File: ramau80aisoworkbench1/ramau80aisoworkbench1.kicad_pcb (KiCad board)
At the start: 2 copper layers, 0 parts

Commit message: mx footprints now sit in proper spots for u80
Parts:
- added C1: C_Small, Capacitor_SMD:C_0805_2012Metric, B.Cu at (266.2, 167.9)
- added C2: 22pF, Capacitor_SMD:C_0805_2012Metric, B.Cu at (291.6, 182.8)
- added C3: 22pF, Capacitor_SMD:C_0805_2012Metric, B.Cu at (280.5, 182.1)
- added C4: 0.1uF, Capacitor_SMD:C_0805_2012Metric, B.Cu at (267.7, 178.2)
- added C5: 0.1uF, Capacitor_SMD:C_0805_2012Metric, B.Cu at (262.1, 178.2)
- added C6: 0.1uF, Capacitor_SMD:C_0805_2012Metric, B.Cu at (256.7, 178.2)
- added C7: 0.1uF, Capacitor_SMD:C_0805_2012Metric, B.Cu at (250.2, 178.2)
- added D_A100: D_Small, Diode_SMD:D_SOD-123, B.Cu at (40.8, 85.3)
- added D_B100: D_Small, Diode_SMD:D_SOD-123, B.Cu at (132.1, 102.0)
- added D_BKSP100: D_Small, Diode_SMD:D_SOD-123, B.Cu at (274.6, 35.8)
- added D_C100: D_Small, Diode_SMD:D_SOD-123, B.Cu at (98.4, 92.1)
- added D_CAPS100: D_Small, Diode_SMD:D_SOD-123, B.Cu at (18.6, 83.7)
- added D_COM100: D_Small, Diode_SMD:D_SOD-123, B.Cu at (190.0, 102.0)
- added D_D100: D_Small, Diode_SMD:D_SOD-123, B.Cu at (80.5, 84.5)
- added D_DEL100: D_Small, Diode_SMD:D_SOD-123, B.Cu at (292.9, 54.7)
- added D_DOWN100: D_Small, Diode_SMD:D_SOD-123, B.Cu at (355.9, 119.4)
- added D_E100: D_Small, Diode_SMD:D_SOD-123, B.Cu at (80.5, 65.5)
- added D_END100: D_Small, Diode_SMD:D_SOD-123, B.Cu at (331.8, 54.8)
- added D_ENT100: D_Small, Diode_SMD:D_SOD-123, B.Cu at (268.6, 69.4)
- added D_EQ100: D_Small, Diode_SMD:D_SOD-123, B.Cu at (245.6, 45.6)
- added D_ESC100: D_Small, Diode_SMD:D_SOD-123, B.Cu at (17.8, 6.98)
- added D_F1: D_Small, Diode_SMD:D_SOD-123, B.Cu at (55.9, 6.98)
- added D_F10: D_Small, Diode_SMD:D_SOD-123, B.Cu at (246.4, 6.98)
- added D_F100: D_Small, Diode_SMD:D_SOD-123, B.Cu at (99.5, 82.9)
- added D_F11: D_Small, Diode_SMD:D_SOD-123, B.Cu at (265.4, 6.98)
- added D_F12: D_Small, Diode_SMD:D_SOD-123, B.Cu at (284.5, 6.98)
- added D_F13: D_Small, Diode_SMD:D_SOD-123, B.Cu at (313.1, 6.98)
- added D_F14: D_Small, Diode_SMD:D_SOD-123, B.Cu at (332.1, 6.98)
- added D_F15: D_Small, Diode_SMD:D_SOD-123, B.Cu at (351.2, 6.98)
- added D_F2: D_Small, Diode_SMD:D_SOD-123, B.Cu at (74.9, 6.86)
- added D_F3: D_Small, Diode_SMD:D_SOD-123, B.Cu at (94.0, 6.98)
- added D_F4: D_Small, Diode_SMD:D_SOD-123, B.Cu at (113.0, 6.98)
- added D_F5: D_Small, Diode_SMD:D_SOD-123, B.Cu at (141.6, 6.98)
- added D_F6: D_Small, Diode_SMD:D_SOD-123, B.Cu at (160.7, 6.98)
- added D_F7: D_Small, Diode_SMD:D_SOD-123, B.Cu at (179.7, 6.98)
- added D_F8: D_Small, Diode_SMD:D_SOD-123, B.Cu at (198.8, 6.98)
- added D_F9: D_Small, Diode_SMD:D_SOD-123, B.Cu at (227.3, 6.98)
- added D_FN100: D_Small, Diode_SMD:D_SOD-123, B.Cu at (313.5, 35.8)
- added D_G100: D_Small, Diode_SMD:D_SOD-123, B.Cu at (118.6, 83.7)
- added D_GRV100: D_Small, Diode_SMD:D_SOD-123, B.Cu at (17.8, 35.6)
- added D_H100: D_Small, Diode_SMD:D_SOD-123, B.Cu at (137.6, 84.5)
- added D_HOME100: D_Small, Diode_SMD:D_SOD-123, B.Cu at (331.8, 35.8)
- added D_I100: D_Small, Diode_SMD:D_SOD-123, B.Cu at (178.1, 65.5)
- added D_J100: D_Small, Diode_SMD:D_SOD-123, B.Cu at (156.7, 84.5)
- added D_K100: D_Small, Diode_SMD:D_SOD-123, B.Cu at (177.3, 84.5)
- added D_L100: D_Small, Diode_SMD:D_SOD-123, B.Cu at (196.4, 84.5)
- added D_LALT100: D_Small, Diode_SMD:D_SOD-123, B.Cu at (45.6, 123.4)
- added D_LCTRL100: D_Small, Diode_SMD:D_SOD-123, B.Cu at (16.2, 123.4)
- added D_LEFT100: D_Small, Diode_SMD:D_SOD-123, B.Cu at (336.9, 119.4)
- added D_LOS100: D_Small, Diode_SMD:D_SOD-123, B.Cu at (76.2, 108.8)
- added D_LSFT100: D_Small, Diode_SMD:D_SOD-123, B.Cu at (16.2, 102.0)
- added D_LSQ100: D_Small, Diode_SMD:D_SOD-123, B.Cu at (237.6, 67.8)
- added D_M100: D_Small, Diode_SMD:D_SOD-123, B.Cu at (171.0, 102.8)
- added D_MIN100: D_Small, Diode_SMD:D_SOD-123, B.Cu at (231.3, 46.4)
- added D_N0: D_Small, Diode_SMD:D_SOD-123, B.Cu at (207.5, 46.4)
- added D_N1: D_Small, Diode_SMD:D_SOD-123, B.Cu at (36.8, 35.6)
- added D_N100: D_Small, Diode_SMD:D_SOD-123, B.Cu at (151.1, 102.8)
- added D_N2: D_Small, Diode_SMD:D_SOD-123, B.Cu at (56.7, 45.6)
- added D_N3: D_Small, Diode_SMD:D_SOD-123, B.Cu at (74.9, 44.8)
- added D_N4: D_Small, Diode_SMD:D_SOD-123, B.Cu at (92.4, 46.4)
- added D_N5: D_Small, Diode_SMD:D_SOD-123, B.Cu at (112.2, 46.4)
- added D_N6: D_Small, Diode_SMD:D_SOD-123, B.Cu at (131.3, 46.4)
- added D_N7: D_Small, Diode_SMD:D_SOD-123, B.Cu at (150.3, 46.4)
- added D_N8: D_Small, Diode_SMD:D_SOD-123, B.Cu at (169.4, 46.4)
- added D_N9: D_Small, Diode_SMD:D_SOD-123, B.Cu at (188.4, 46.4)
- added D_O100: D_Small, Diode_SMD:D_SOD-123, B.Cu at (199.5, 65.5)
- added D_P100: D_Small, Diode_SMD:D_SOD-123, B.Cu at (217.8, 65.5)
- added D_PER100: D_Small, Diode_SMD:D_SOD-123, B.Cu at (207.5, 102.8)
- added D_PGDN100: D_Small, Diode_SMD:D_SOD-123, B.Cu at (350.8, 54.8)
- added D_PGUP100: D_Small, Diode_SMD:D_SOD-123, B.Cu at (351.6, 34.9)
- added D_PIPE100: D_Small, Diode_SMD:D_SOD-123, B.Cu at (260.7, 83.7)
- added D_Q100: D_Small, Diode_SMD:D_SOD-123, B.Cu at (51.1, 54.5)
- added D_QUO100: D_Small, Diode_SMD:D_SOD-123, B.Cu at (241.6, 85.3)
- added D_R100: D_Small, Diode_SMD:D_SOD-123, B.Cu at (100.3, 64.7)
- added D_RALT100: D_Small, Diode_SMD:D_SOD-123, B.Cu at (255.9, 122.6)
- added D_RCTRL100: D_Small, Diode_SMD:D_SOD-123, B.Cu at (282.9, 122.6)
- added D_RIGHT100: D_Small, Diode_SMD:D_SOD-123, B.Cu at (375.0, 119.4)
- added D_ROS100: D_Small, Diode_SMD:D_SOD-123, B.Cu at (225.7, 122.6)
- added D_RSFT100: D_Small, Diode_SMD:D_SOD-123, B.Cu at (271.8, 102.8)
- added D_RSQ100: D_Small, Diode_SMD:D_SOD-123, B.Cu at (261.3, 54.4)
- added D_S100: D_Small, Diode_SMD:D_SOD-123, B.Cu at (59.1, 84.5)
- added D_SEMI100: D_Small, Diode_SMD:D_SOD-123, B.Cu at (216.2, 84.5)
- added D_SLASH100: D_Small, Diode_SMD:D_SOD-123, B.Cu at (225.7, 103.6)
- added D_SPACE100: D_Small, Diode_SMD:D_SOD-123, B.Cu at (154.0, 111.9)
- added D_T100: D_Small, Diode_SMD:D_SOD-123, B.Cu at (118.6, 65.5)
- added D_TAB100: D_Small, Diode_SMD:D_SOD-123, B.Cu at (18.6, 65.5)
- added D_TILD100: D_Small, Diode_SMD:D_SOD-123, B.Cu at (34.4, 102.0)
- added D_U100: D_Small, Diode_SMD:D_SOD-123, B.Cu at (158.3, 64.6)
- added D_UP100: D_Small, Diode_SMD:D_SOD-123, B.Cu at (332.6, 92.9)
- added D_V100: D_Small, Diode_SMD:D_SOD-123, B.Cu at (113.8, 102.0)
- added D_W100: D_Small, Diode_SMD:D_SOD-123, B.Cu at (61.4, 65.5)
- added D_X100: D_Small, Diode_SMD:D_SOD-123, B.Cu at (79.4, 92.8)
- added D_Y100: D_Small, Diode_SMD:D_SOD-123, B.Cu at (138.4, 64.7)
- added D_Z100: D_Small, Diode_SMD:D_SOD-123, B.Cu at (54.3, 101.2)
- added F1: 500mA, Fuse:Fuse_1206_3216Metric, B.Cu at (287.7, 167.9)
- added MX_A100: MX-NoLED, MX_Only:MXOnly-1U, F.Cu at (42.9, 76.2)
- added MX_B100: MX-NoLED, MX_Only:MXOnly-1U, F.Cu at (128.6, 95.2)
- added MX_BKSP100: MX-NoLED, MX_Only:MXOnly-1U, F.Cu at (266.7, 38.1)
- added MX_C100: MX-NoLED, MX_Only:MXOnly-1U, F.Cu at (90.5, 95.2)
- added MX_CAPS100: MX-NoLED, MX_Only:MXOnly-1U, F.Cu at (16.7, 76.2)
- added MX_COM100: MX-NoLED, MX_Only:MXOnly-1U, F.Cu at (185.7, 95.2)
- added MX_D100: MX-NoLED, MX_Only:MXOnly-1U, F.Cu at (81.0, 76.2)
- added MX_DEL100: MX-NoLED, MX_Only:MXOnly-1U, F.Cu at (304.8, 57.1)
- added MX_DOWN100: MX-NoLED, MX_Only:MXOnly-1U, F.Cu at (323.9, 114.3)
- added MX_E100: MX-NoLED, MX_Only:MXOnly-1U, F.Cu at (76.2, 57.1)
- added MX_END100: MX-NoLED, MX_Only:MXOnly-1U, F.Cu at (323.9, 57.1)
- added MX_ENT100: MX-ISO-ENT, MX_Only:MXOnly-1U, F.Cu at (276.2, 66.7)
- added MX_EQ100: MX-NoLED, MX_Only:MXOnly-1U, F.Cu at (238.1, 38.1)
- added MX_ESC100: MX-NoLED, MX_Only:MXOnly-1U, F.Cu at (9.53, 9.53)
- added MX_F1: MX-NoLED, MX_Only:MXOnly-1U, F.Cu at (47.6, 9.53)
- added MX_F10: MX-NoLED, MX_Only:MXOnly-1U, F.Cu at (238.1, 9.53)
- added MX_F100: MX-NoLED, MX_Only:MXOnly-1U, F.Cu at (100.0, 76.2)
- added MX_F11: MX-NoLED, MX_Only:MXOnly-1U, F.Cu at (257.2, 9.53)
- added MX_F12: MX-NoLED, MX_Only:MXOnly-1U, F.Cu at (276.2, 9.53)
- added MX_F13: MX-NoLED, MX_Only:MXOnly-1U, F.Cu at (304.8, 9.53)
- added MX_F14: MX-NoLED, MX_Only:MXOnly-1U, F.Cu at (323.9, 9.53)
- added MX_F15: MX-NoLED, MX_Only:MXOnly-1U, F.Cu at (342.9, 9.53)
- added MX_F2: MX-NoLED, MX_Only:MXOnly-1U, F.Cu at (66.7, 9.53)
- added MX_F3: MX-NoLED, MX_Only:MXOnly-1U, F.Cu at (85.7, 9.53)
- added MX_F4: MX-NoLED, MX_Only:MXOnly-1U, F.Cu at (104.8, 9.53)
- added MX_F5: MX-NoLED, MX_Only:MXOnly-1U, F.Cu at (133.3, 9.53)
- added MX_F6: MX-NoLED, MX_Only:MXOnly-1U, F.Cu at (152.4, 9.53)
- added MX_F7: MX-NoLED, MX_Only:MXOnly-1U, F.Cu at (171.4, 9.53)
- added MX_F8: MX-NoLED, MX_Only:MXOnly-1U, F.Cu at (190.5, 9.53)
- added MX_F9: MX-NoLED, MX_Only:MXOnly-1U, F.Cu at (219.1, 9.53)
- added MX_FN100: MX-NoLED, MX_Only:MXOnly-1U, F.Cu at (304.8, 38.1)
- added MX_G100: MX-NoLED, MX_Only:MXOnly-1U, F.Cu at (119.1, 76.2)
- added MX_GRV100: MX-NoLED, MX_Only:MXOnly-1U, F.Cu at (9.53, 38.1)
- added MX_H100: MX-NoLED, MX_Only:MXOnly-1U, F.Cu at (138.1, 76.2)
- added MX_HOME100: MX-NoLED, MX_Only:MXOnly-1U, F.Cu at (323.9, 38.1)
- added MX_I100: MX-NoLED, MX_Only:MXOnly-1U, F.Cu at (171.4, 57.1)
- added MX_J100: MX-NoLED, MX_Only:MXOnly-1U, F.Cu at (157.2, 76.2)
- added MX_K100: MX-NoLED, MX_Only:MXOnly-1U, F.Cu at (176.2, 76.2)
- added MX_L100: MX-NoLED, MX_Only:MXOnly-1U, F.Cu at (195.3, 76.2)
- added MX_LALT100: MX-NoLED, MX_Only:MXOnly-1U, F.Cu at (38.1, 114.3)
- added MX_LCTRL100: MX-NoLED, MX_Only:MXOnly-1U, F.Cu at (14.3, 114.3)
- added MX_LEFT100: MX-NoLED, MX_Only:MXOnly-1U, F.Cu at (304.8, 114.3)
- added MX_LOS100: MX-NoLED, MX_Only:MXOnly-1U, F.Cu at (61.9, 114.3)
- added MX_LSFT100: MX-NoLED, MX_Only:MXOnly-1U, F.Cu at (11.9, 95.2)
- added MX_LSQ100: MX-NoLED, MX_Only:MXOnly-1U, F.Cu at (228.6, 57.1)
- added MX_M100: MX-NoLED, MX_Only:MXOnly-1U, F.Cu at (166.7, 95.2)
- added MX_MIN100: MX-NoLED, MX_Only:MXOnly-1U, F.Cu at (219.1, 38.1)
- added MX_N0: MX-NoLED, MX_Only:MXOnly-1U, F.Cu at (200.0, 38.1)
- added MX_N1: MX-NoLED, MX_Only:MXOnly-1U, F.Cu at (28.6, 38.1)
- added MX_N100: MX-NoLED, MX_Only:MXOnly-1U, F.Cu at (147.6, 95.2)
- added MX_N2: MX-NoLED, MX_Only:MXOnly-1U, F.Cu at (47.6, 38.1)
- added MX_N3: MX-NoLED, MX_Only:MXOnly-1U, F.Cu at (66.7, 38.1)
- added MX_N4: MX-NoLED, MX_Only:MXOnly-1U, F.Cu at (85.7, 38.1)
- added MX_N5: MX-NoLED, MX_Only:MXOnly-1U, F.Cu at (104.8, 38.1)
- added MX_N6: MX-NoLED, MX_Only:MXOnly-1U, F.Cu at (123.8, 38.1)
- added MX_N7: MX-NoLED, MX_Only:MXOnly-1U, F.Cu at (142.9, 38.1)
- added MX_N8: MX-NoLED, MX_Only:MXOnly-1U, F.Cu at (161.9, 38.1)
- added MX_N9: MX-NoLED, MX_Only:MXOnly-1U, F.Cu at (181.0, 38.1)
- added MX_O100: MX-NoLED, MX_Only:MXOnly-1U, F.Cu at (190.5, 57.1)
- added MX_P100: MX-NoLED, MX_Only:MXOnly-1U, F.Cu at (209.6, 57.1)
- added MX_PER100: MX-NoLED, MX_Only:MXOnly-1U, F.Cu at (204.8, 95.2)
- added MX_PGDN100: MX-NoLED, MX_Only:MXOnly-1U, F.Cu at (342.9, 57.1)
- added MX_PGUP100: MX-NoLED, MX_Only:MXOnly-1U, F.Cu at (342.9, 38.1)
- added MX_PIPE100: MX-NoLED, MX_Only:MXOnly-1U, F.Cu at (252.4, 76.2)
- added MX_Q100: MX-NoLED, MX_Only:MXOnly-1U, F.Cu at (38.1, 57.1)
- added MX_QUO100: MX-NoLED, MX_Only:MXOnly-1U, F.Cu at (233.4, 76.2)
- added MX_R100: MX-NoLED, MX_Only:MXOnly-1U, F.Cu at (95.2, 57.1)
- added MX_RALT100: MX-NoLED, MX_Only:MXOnly-1U, F.Cu at (247.7, 114.3)
- added MX_RCTRL100: MX-NoLED, MX_Only:MXOnly-1U, F.Cu at (271.5, 114.3)
- added MX_RIGHT100: MX-NoLED, MX_Only:MXOnly-1U, F.Cu at (342.9, 114.3)
- added MX_ROS100: MX-NoLED, MX_Only:MXOnly-1U, F.Cu at (223.8, 114.3)
- added MX_RSFT100: MX-NoLED, MX_Only:MXOnly-1U, F.Cu at (257.2, 95.2)
- added MX_RSQ100: MX-NoLED, MX_Only:MXOnly-1U, F.Cu at (247.7, 57.1)
- added MX_S100: MX-NoLED, MX_Only:MXOnly-1U, F.Cu at (61.9, 76.2)
- added MX_SEMI100: MX-NoLED, MX_Only:MXOnly-1U, F.Cu at (214.3, 76.2)
- added MX_SLASH100: MX-NoLED, MX_Only:MXOnly-1U, F.Cu at (223.8, 95.2)
- added MX_SPACE100: MX-NoLED, MX_Only:MXOnly-1U, F.Cu at (145.3, 114.3)
- added MX_T100: MX-NoLED, MX_Only:MXOnly-1U, F.Cu at (114.3, 57.1)
- added MX_TAB100: MX-NoLED, MX_Only:MXOnly-1U, F.Cu at (14.3, 57.1)
- added MX_TILD100: MX-NoLED, MX_Only:MXOnly-1U, F.Cu at (33.3, 95.2)
- added MX_U100: MX-NoLED, MX_Only:MXOnly-1U, F.Cu at (152.4, 57.1)
- added MX_UP100: MX-NoLED, MX_Only:MXOnly-1U, F.Cu at (323.9, 95.2)
- added MX_V100: MX-NoLED, MX_Only:MXOnly-1U, F.Cu at (109.5, 95.2)
- added MX_W100: MX-NoLED, MX_Only:MXOnly-1U, F.Cu at (57.1, 57.1)
- added MX_X100: MX-NoLED, MX_Only:MXOnly-1U, F.Cu at (71.4, 95.2)
- added MX_Y100: MX-NoLED, MX_Only:MXOnly-1U, F.Cu at (133.3, 57.1)
- added MX_Z100: MX-NoLED, MX_Only:MXOnly-1U, F.Cu at (52.4, 95.2)
- added R1: 22, Resistor_SMD:R_0805_2012Metric, B.Cu at (331.2, 198.8)
- added R2: 22, Resistor_SMD:R_0805_2012Metric, B.Cu at (325.0, 198.8)
- added R3: 10k, Resistor_SMD:R_0805_2012Metric, B.Cu at (273.5, 179.8)
- added R4: 10k, Resistor_SMD:R_0805_2012Metric, B.Cu at (284.5, 160.7)
- added SW1: SW_PUSH, random-keyboard-parts:SKQG-1155865, B.Cu at (293.2, 175.8)
- added U1: ATmega32U4-AU, Package_QFP:TQFP-44_10x10mm_P0.8mm, B.Cu at (275.7, 169.4)
- added USB1: Molex-0548190589, random-keyboard-parts:PJ-3200B-4A-Assembly, F.Cu at (332.9, 173.4)
- added Y1: 16MHz, Crystal:Crystal_SMD_3225-4Pin_3.2x2.5mm, B.Cu at (285.3, 181.4)

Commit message: diodes aligned to switches
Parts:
- moved D_DOWN100 25.0 mm to (332.1, 111.8)
- moved D_LEFT100 25.0 mm to (313.1, 111.8)
- moved D_RIGHT100 25.0 mm to (351.2, 111.8)
- moved D_DEL100 20.2 mm to (313.1, 54.6)
- moved D_A100 15.6 mm to (51.2, 73.7)
- moved D_S100 15.6 mm to (70.2, 73.7)
- moved D_H100 14.0 mm to (146.4, 73.7)
- moved D_D100 14.0 mm to (89.3, 73.7)
- moved D_J100 14.0 mm to (165.5, 73.7)
- moved D_G100 13.4 mm to (127.4, 73.7)
- moved D_LCTRL100 13.3 mm to (22.6, 111.8)
- moved D_LSQ100 13.3 mm to (236.9, 54.6)
- moved D_K100 13.0 mm to (184.5, 73.7)
- moved D_L100 13.0 mm to (203.6, 73.7)
- moved D_F100 12.8 mm to (108.3, 73.7)
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
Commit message: fixed error in footprint assignment. updated switch footprints to use appropriate size, ditched leds
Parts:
- C1: value C_Small -> 1uF
- MX_A100, MX_B100, MX_C100, MX_COM100, MX_D100, MX_DEL100, MX_DOWN100, MX_E100, MX_END100, MX_EQ100, MX_ESC100, MX_F1, MX_F10, MX_F100, MX_F11, MX_F12, MX_F13, MX_F14, MX_F15, MX_F2, MX_F3, MX_F4, MX_F5, MX_F6, MX_F7, MX_F8, MX_F9, MX_FN100, MX_G100, MX_GRV100, MX_H100, MX_HOME100, MX_I100, MX_J100, MX_K100, MX_L100, MX_LALT100, MX_LEFT100, MX_LSQ100, MX_M100, MX_MIN100, MX_N0, MX_N1, MX_N100, MX_N2, MX_N3, MX_N4, MX_N5, MX_N6, MX_N7, MX_N8, MX_N9, MX_O100, MX_P100, MX_PER100, MX_PGDN100, MX_PGUP100, MX_PIPE100, MX_Q100, MX_QUO100, MX_R100, MX_RALT100, MX_RIGHT100, MX_RSQ100, MX_S100, MX_SEMI100, MX_SLASH100, MX_T100, MX_TILD100, MX_U100, MX_UP100, MX_V100, MX_W100, MX_X100, MX_Y100, MX_Z100: footprint MX_Only:MXOnly-1U -> MX_Only:MXOnly-1U-NoLED
- MX_BKSP100: footprint MX_Only:MXOnly-1U -> MX_Only:MXOnly-2U-NoLED
- MX_CAPS100: footprint MX_Only:MXOnly-1U -> MX_Only:MXOnly-1.75U-NoLED
- MX_ENT100: footprint MX_Only:MXOnly-1U -> MX_Only:MXOnly-ISO-ROTATED-NoLED
- MX_LCTRL100, MX_LOS100, MX_RCTRL100, MX_ROS100, MX_TAB100: footprint MX_Only:MXOnly-1U -> MX_Only:MXOnly-1.5U-NoLED
- MX_LSFT100: footprint MX_Only:MXOnly-1U -> MX_Only:MXOnly-1.25U-NoLED
- MX_RSFT100: footprint MX_Only:MXOnly-1U -> MX_Only:MXOnly-2.75U-NoLED
- MX_SPACE100: footprint MX_Only:MXOnly-1U -> MX_Only:MXOnly-7U-NoLED
- USB1: footprint random-keyboard-parts:PJ-3200B-4A-Assembly -> random-keyboard-parts:Molex-0548190589
- moved USB1 388.2 mm to (-23.1, 18.5)
- moved R2 356.0 mm to (14.7, 24.2)
- moved R1 356.0 mm to (20.9, 24.2)
- moved C2 321.6 mm to (24.4, 3.81), turned to 270 degrees
- moved Y1 311.6 mm to (29.2, 3.81), turned to 180 degrees
- moved C3 304.2 mm to (34.0, 3.78), turned to 90 degrees
- moved U1 291.2 mm to (28.4, 15.7)
- moved R4 283.4 mm to (36.8, 22.9), turned to 90 degrees
- moved C7 266.4 mm to (32.3, 24.9), turned to 180 degrees
- moved R3 17.5 mm to (289.9, 185.9)
- moved MX_ENT100 2.38 mm to (273.8, 66.7), turned to 0 degrees
- moved MX_RSFT100 2.38 mm to (259.6, 95.2)

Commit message: re-aligned spacebar. wups.
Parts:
- moved C1 383.3 mm to (-48.9, -50.4)
- moved C4 383.3 mm to (-47.5, -40.1)
- moved C5 383.3 mm to (-53.0, -40.1)
- moved C6 383.3 mm to (-58.4, -40.1)
- moved F1 383.3 mm to (-27.5, -50.4)
- moved R3 383.3 mm to (-25.2, -32.4)
- moved SW1 383.3 mm to (-21.9, -42.5)
- moved D_SPACE100 2.41 mm to (151.1, 111.8)
- moved MX_SPACE100 2.38 mm to (142.9, 114.3)

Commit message: lee. updated to kicad 7. adding usbc library
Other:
- net class Default removed

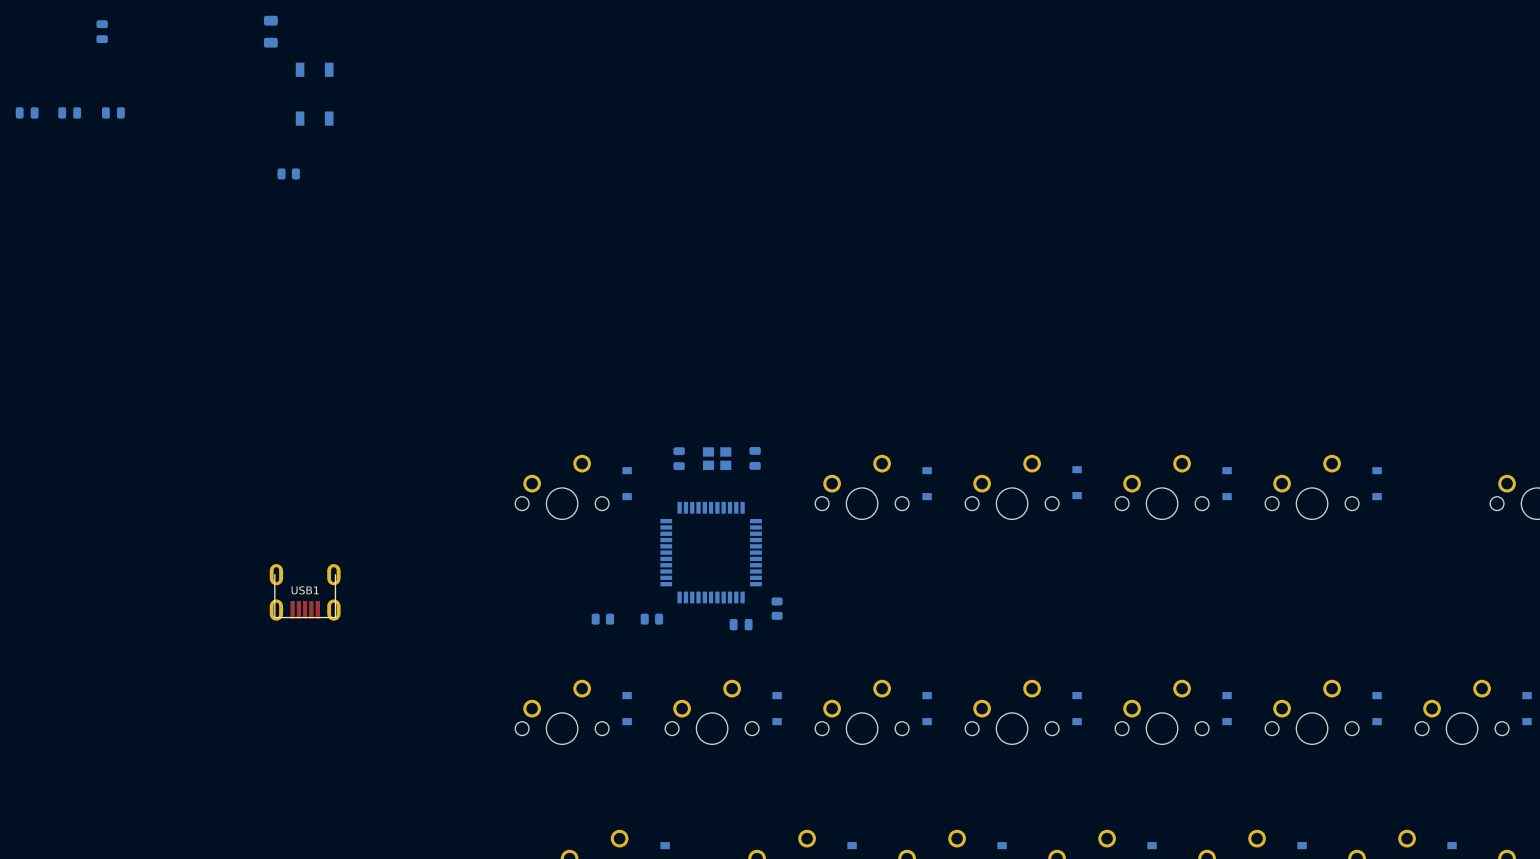
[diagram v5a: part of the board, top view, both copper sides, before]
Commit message: all parts on board! lets make sure the resistors and capacitors are all right and that the ground issue is sorted. then routing
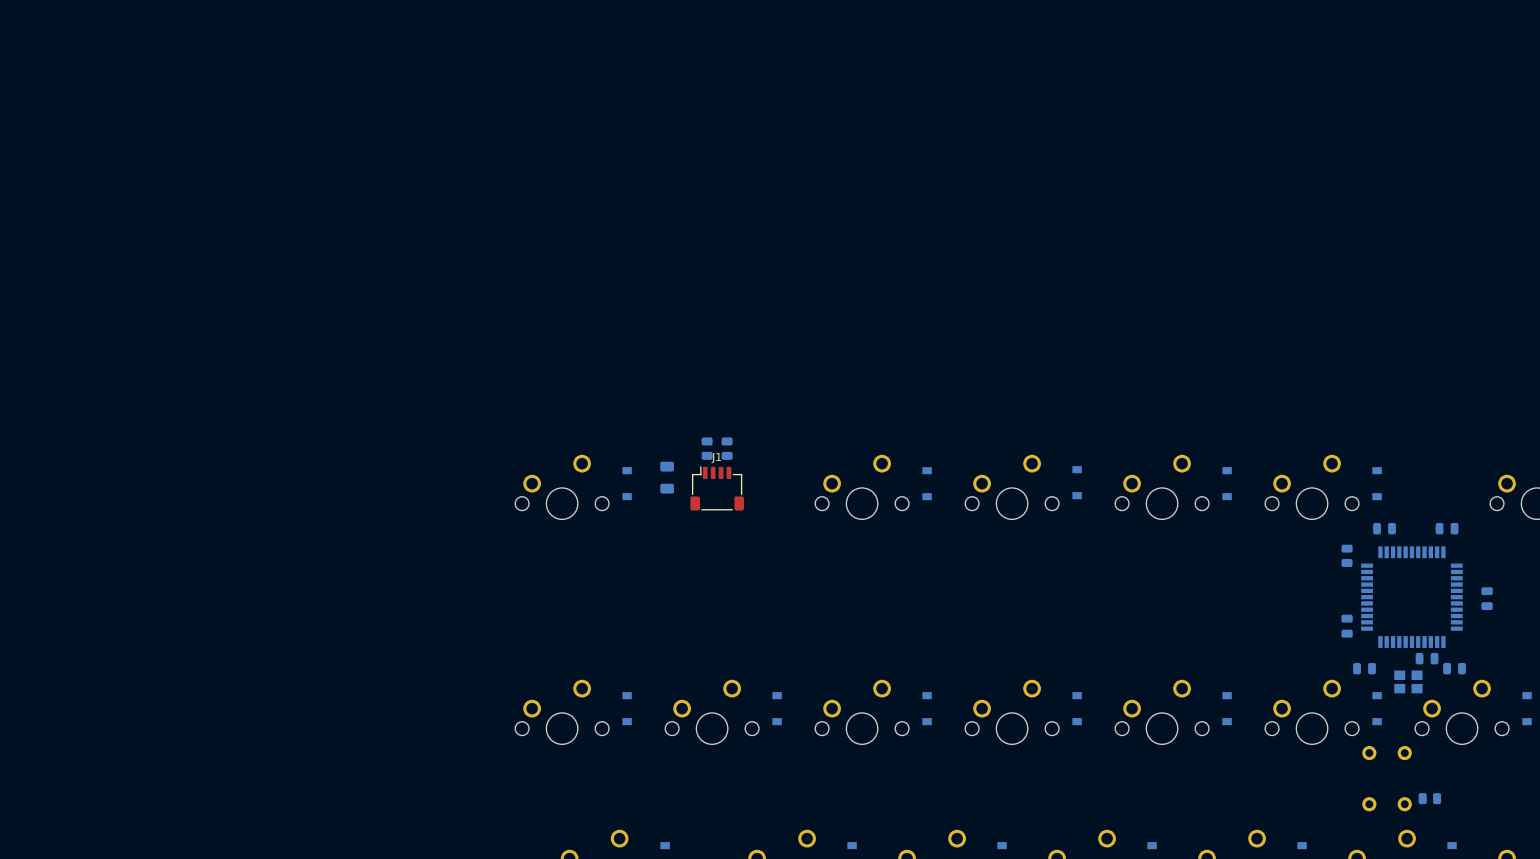
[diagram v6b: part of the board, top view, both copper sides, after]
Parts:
- removed USB1: Molex-0548190589, random-keyboard-parts:Molex-0548190589
- added J1: Conn_01x04_Socket, Connector_JST:JST_SH_SM04B-SRSS-TB_1x04-1MP_P1.00mm_Horizontal, F.Cu at (29.2, 7.62)
- SW1: footprint random-keyboard-parts:SKQG-1155865 -> random-keyboard-parts:PushButton_6x6mm_TH_Pretty
- moved C1 190.1 mm to (127.0, 21.6)
- moved C5 185.8 mm to (119.4, 29.2)
- moved C6 179.9 mm to (109.2, 25.1), turned to 90 degrees
- moved C4 169.9 mm to (114.0, 12.7)
- moved R3 165.2 mm to (119.7, 47.0)
- moved SW1 161.6 mm to (114.3, 44.5), turned to -90 degrees
- moved C2 102.0 mm to (122.9, 30.5), turned to 0 degrees
- moved Y1 92.3 mm to (117.0, 32.2), turned to 0 degrees
- moved C7 90.5 mm to (121.9, 12.7), turned to 0 degrees
- moved U1 89.2 mm to (117.5, 21.4), turned to 180 degrees
- moved C3 81.9 mm to (111.4, 30.5), turned to 0 degrees
- moved F1 75.8 mm to (22.9, 6.22), turned to -90 degrees
- moved R4 72.7 mm to (109.2, 16.2), turned to -90 degrees
- moved R2 26.8 mm to (30.5, 2.54), turned to -90 degrees
- moved R1 22.8 mm to (27.9, 2.54), turned to 90 degrees
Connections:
- U1 pad 1: Net-(U1-Pad1) -> unconnected-(U1-PE6-Pad1)
- U1 pad 10: Net-(U1-Pad10) -> unconnected-(U1-PB2-Pad10)
- U1 pad 11: Net-(U1-Pad11) -> unconnected-(U1-PB3-Pad11)
- U1 pad 12: Net-(U1-Pad12) -> unconnected-(U1-PB7-Pad12)
- U1 pad 18: Net-(U1-Pad18) -> unconnected-(U1-PD0-Pad18)
- U1 pad 19: Net-(U1-Pad19) -> unconnected-(U1-PD1-Pad19)
- U1 pad 20: Net-(U1-Pad20) -> unconnected-(U1-PD2-Pad20)
- U1 pad 21: Net-(U1-Pad21) -> unconnected-(U1-PD3-Pad21)
- U1 pad 22: Net-(U1-Pad22) -> unconnected-(U1-PD5-Pad22)
- U1 pad 25: Net-(U1-Pad25) -> unconnected-(U1-PD4-Pad25)
- U1 pad 26: Net-(U1-Pad26) -> unconnected-(U1-PD6-Pad26)
- U1 pad 27: Net-(U1-Pad27) -> unconnected-(U1-PD7-Pad27)
- U1 pad 28: Net-(U1-Pad28) -> unconnected-(U1-PB4-Pad28)
- U1 pad 29: Net-(U1-Pad29) -> unconnected-(U1-PB5-Pad29)
- U1 pad 30: Net-(U1-Pad30) -> unconnected-(U1-PB6-Pad30)
- U1 pad 31: Net-(U1-Pad31) -> unconnected-(U1-PC6-Pad31)
- U1 pad 32: Net-(U1-Pad32) -> unconnected-(U1-PC7-Pad32)
- U1 pad 36: Net-(U1-Pad36) -> unconnected-(U1-PF7-Pad36)
- U1 pad 37: Net-(U1-Pad37) -> unconnected-(U1-PF6-Pad37)
- U1 pad 38: Net-(U1-Pad38) -> unconnected-(U1-PF5-Pad38)
- U1 pad 39: Net-(U1-Pad39) -> unconnected-(U1-PF4-Pad39)
- U1 pad 40: Net-(U1-Pad40) -> unconnected-(U1-PF1-Pad40)
- U1 pad 41: Net-(U1-Pad41) -> unconnected-(U1-PF0-Pad41)
- U1 pad 42: Net-(U1-Pad42) -> unconnected-(U1-AREF-Pad42)
- U1 pad 8: Net-(U1-Pad8) -> unconnected-(U1-PB0-Pad8)
- U1 pad 9: Net-(U1-Pad9) -> unconnected-(U1-PB1-Pad9)

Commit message: added traces
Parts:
- moved C3 21.6 mm to (133.1, 31.2)
- moved Y1 16.6 mm to (132.8, 27.1), turned to 90 degrees
- moved C2 12.3 mm to (132.8, 23.2)
- moved C5 3.09 mm to (120.7, 32.0)
- moved D_RSFT100 1.89 mm to (267.0, 91.7)
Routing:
- net ROW5: track 0.00 -> 469.6 mm, vias 0 -> 4
- net ROW0: track 0.00 -> 457.7 mm, vias 0 -> 28
- net ROW4: track 0.00 -> 422.3 mm, vias 0 -> 28
- net ROW3: track 0.00 -> 399.8 mm, vias 0 -> 28
- net ROW1: track 0.00 -> 338.4 mm, vias 0 -> 28
- net ROW2: track 0.00 -> 332.5 mm, vias 0 -> 28
- net COL10: track 0.00 -> 230.2 mm
- net COL11: track 0.00 -> 229.8 mm
- net COL9: track 0.00 -> 213.8 mm
- net COL13: track 0.00 -> 210.5 mm
- net COL12: track 0.00 -> 209.9 mm
- net COL8: track 0.00 -> 199.7 mm
- net COL7: track 0.00 -> 193.7 mm
- net +5V: track 0.00 -> 163.4 mm, vias 0 -> 6
- net COL14: track 0.00 -> 162.7 mm
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- added copper zone on B.Cu, net GND
- added copper zone on F.Cu, net GND
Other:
- board outline added: 357.5 x 128.8 mm
